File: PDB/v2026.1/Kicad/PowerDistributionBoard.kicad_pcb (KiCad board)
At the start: 2 copper layers, 171 x 112.4 mm, 75 parts, among them J1 12V_EXP3, J10 BMS, J11 IMD, J12 Suspension_Linear_Pot1, J13 Suspension_Linear_Pot2, J14 Suspension_Linear_Pot3, J15 Suspension_Linear_Pot4, J16 CCM_Faults, J17 EXP1_5V, J18 RasPI_5V, J19 LATCH_12V, J2 12V_EXP2, J20 Throttle_Sensor, J21 Current_Sensor, J24 Wheel_Sensor1, J25 Wheel_Sensor2, J26 3V3_EXP, J27 BATTERY_12V, J28 BATTERY_GND, J29 BATTERY_24V, J3 12V_EXP1, J31 FAN1_24V, J32 FAN2_24V, J33 PUMP1_24V, J34 PUMP2_24V, J35 24V_EXP1, J4 RTM, J5 CCM_12V, J7 BSPD, J8 LATCH, J9 TSSI, U1 5to3.3_Linear_Regulator, U2 TLV76150DCYR

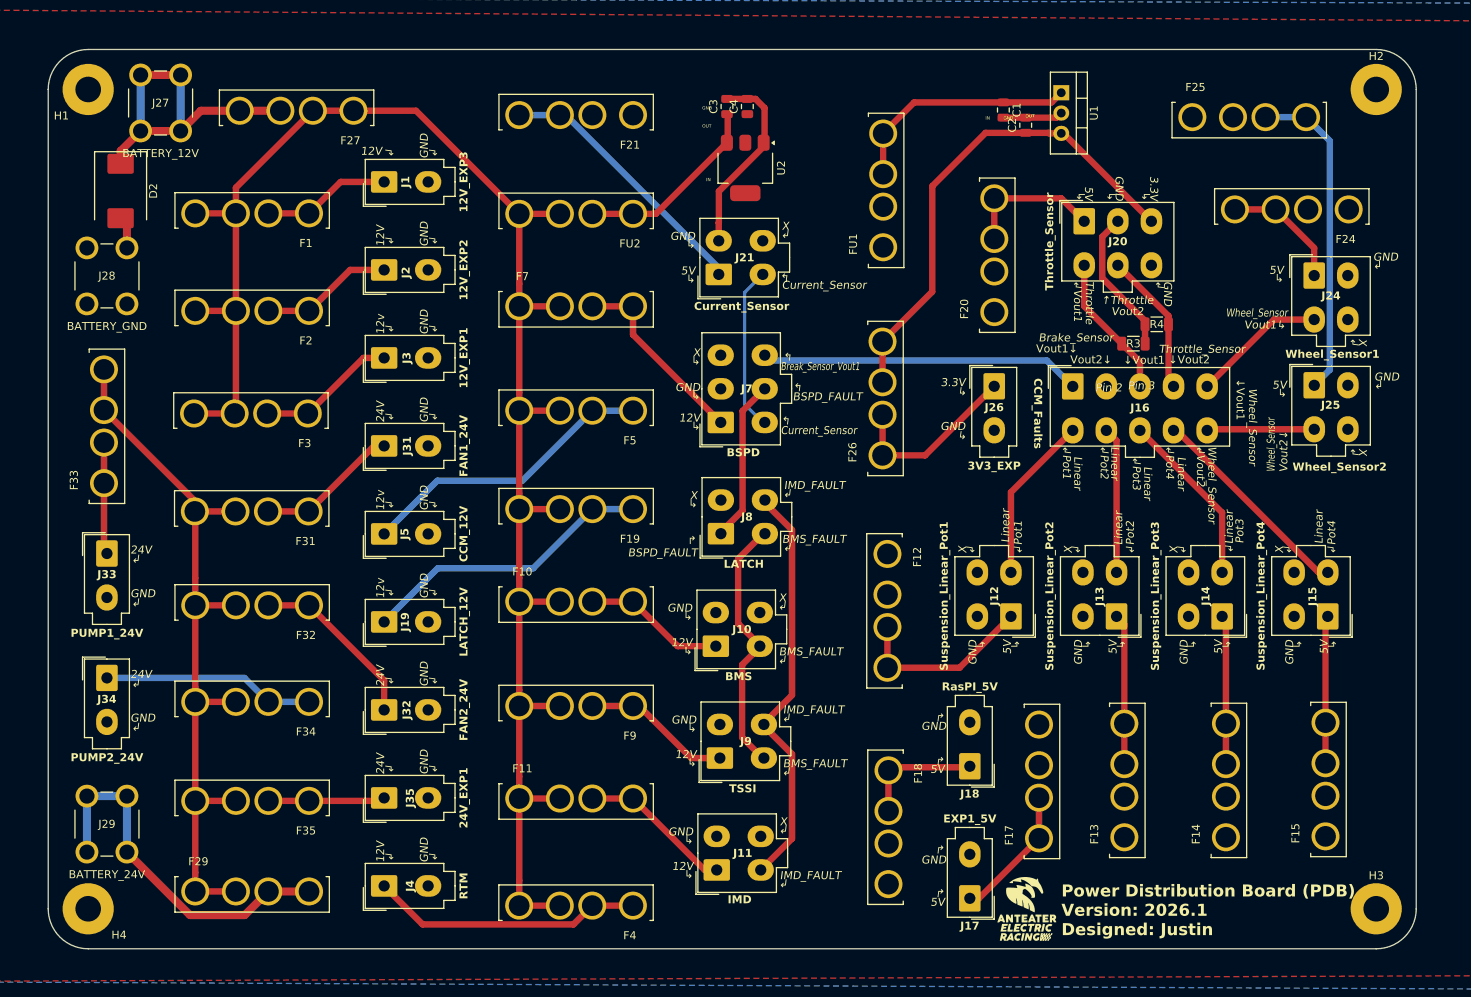
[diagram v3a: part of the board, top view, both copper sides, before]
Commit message: Shink overall board size for PDB
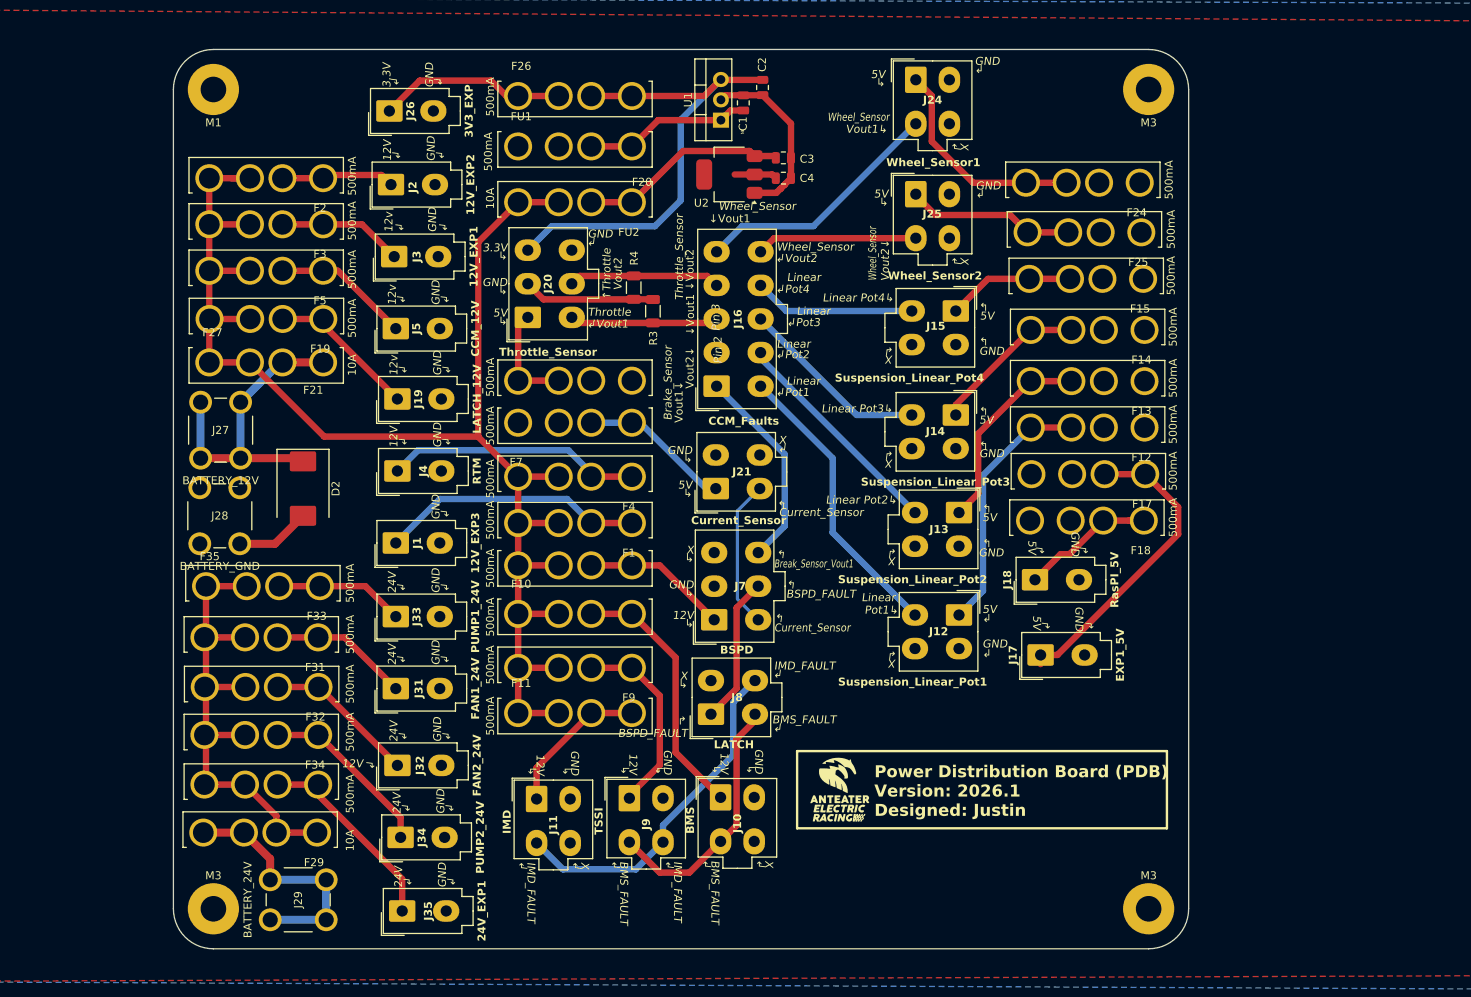
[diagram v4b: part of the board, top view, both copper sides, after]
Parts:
- added REF**: kirby, 0footprints:kirby, B.Cu at (116.1, 90.2)
- moved J26 83.1 mm to (92.8, 32.0), turned to 90 degrees
- moved J20 70.6 mm to (110.1, 57.8), turned to 90 degrees
- moved F15 69.9 mm to (179.9, 52.6), turned to 180 degrees
- moved R4 65.5 mm to (123.3, 54.1), turned to -90 degrees
- moved R3 60.2 mm to (125.7, 57.0), turned to 90 degrees
- moved J15 60.2 mm to (163.6, 57.0), turned to -90 degrees
- moved F14 59.4 mm to (180.1, 59.0), turned to 180 degrees
- moved F1 55.9 mm to (116.0, 83.1)
- moved J24 55.5 mm to (158.6, 28.1)
- moved J25 55.2 mm to (158.6, 42.4)
- moved F20 55.0 mm to (116.0, 65.3), turned to 180 degrees
- moved F26 53.9 mm to (116.0, 30.5), turned to 0 degrees
- moved F4 53.6 mm to (116.0, 77.3)
- moved J4 51.9 mm to (93.8, 77.0)
- moved F13 50.5 mm to (180.1, 65.4), turned to 180 degrees
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- renumbered H1 to M1, H4 to M3, H2 to M3, H3 to M3
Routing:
- net 24V: track 95.4 -> 63.0 mm
- net 12V: track 215.4 -> 187.9 mm
- net /Fuse_EXP1_5V: track 16.8 -> 38.9 mm
- net /Fuse_CCM_12V: track 37.5 -> 17.2 mm
- net /Fuse_Wheel2: track 40.6 -> 21.1 mm
- net /Fuse_LATCH_12V: track 36.9 -> 19.7 mm
- net /Fuse_EXP3_12V: track 16.1 -> 33.0 mm
- net Linear_Pot1: track 20.9 -> 36.6 mm
- net /Fuse_BMMS: track 17.7 -> 33.1 mm
- net /Fuse_Batt24V: track 46.2 -> 31.3 mm
- net Wheel_Sensor_Vout1: track 16.8 -> 31.5 mm
- net /Fuse_CurrentSensor: track 33.7 -> 19.0 mm
- net Brake_Sensor_Vout1: track 40.1 -> 25.7 mm
- net /Fuse_Wheel1: track 16.2 -> 27.5 mm
- net /Fuse_EXP1_24V: track 15.2 -> 25.2 mm
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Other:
- board size 171 x 112.4 mm -> 126.9 x 112.4 mm
- board text removed: "GND"
- board text removed: "OUT"

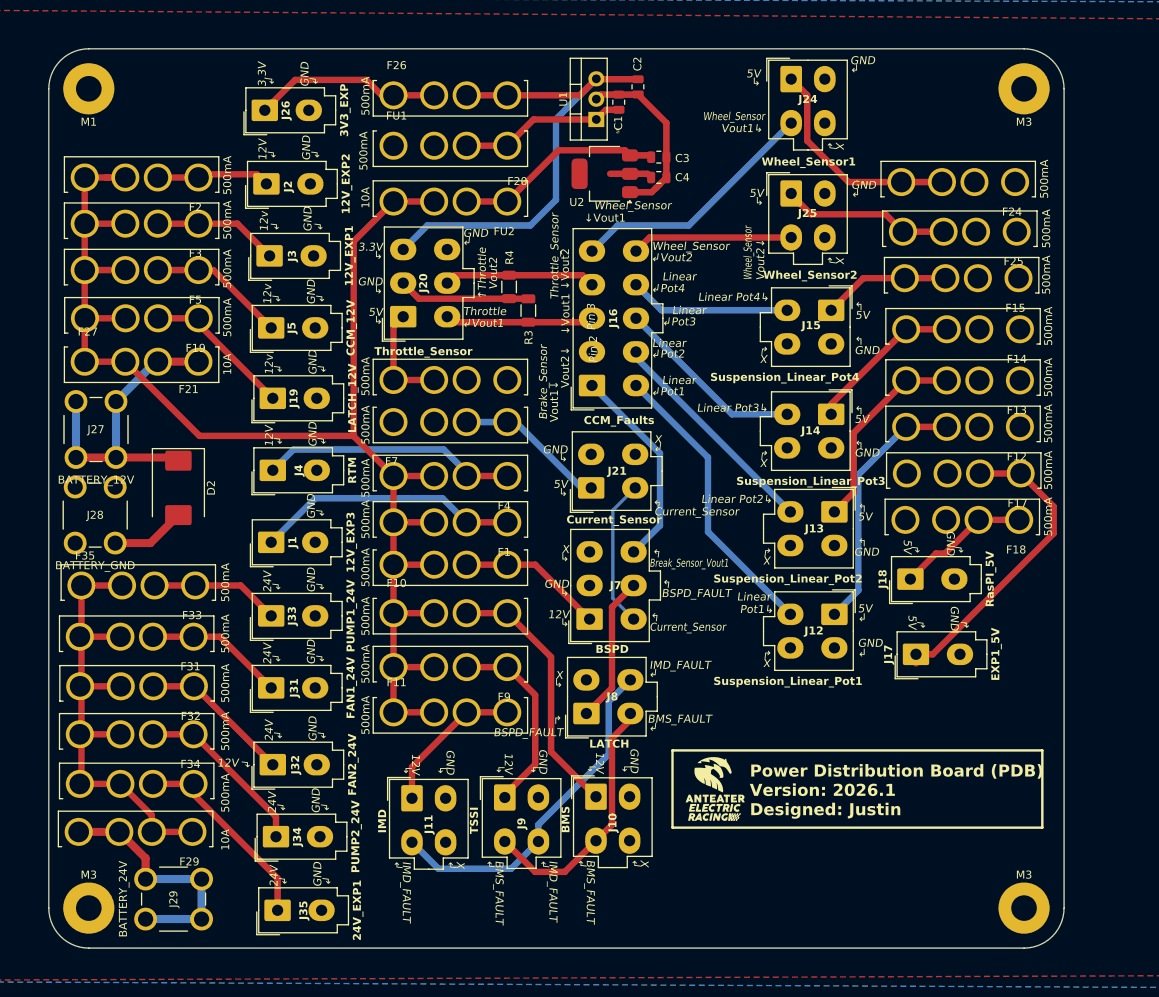
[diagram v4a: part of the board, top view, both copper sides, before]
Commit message: PDB: Removed most 5V fuses, made board size smaller
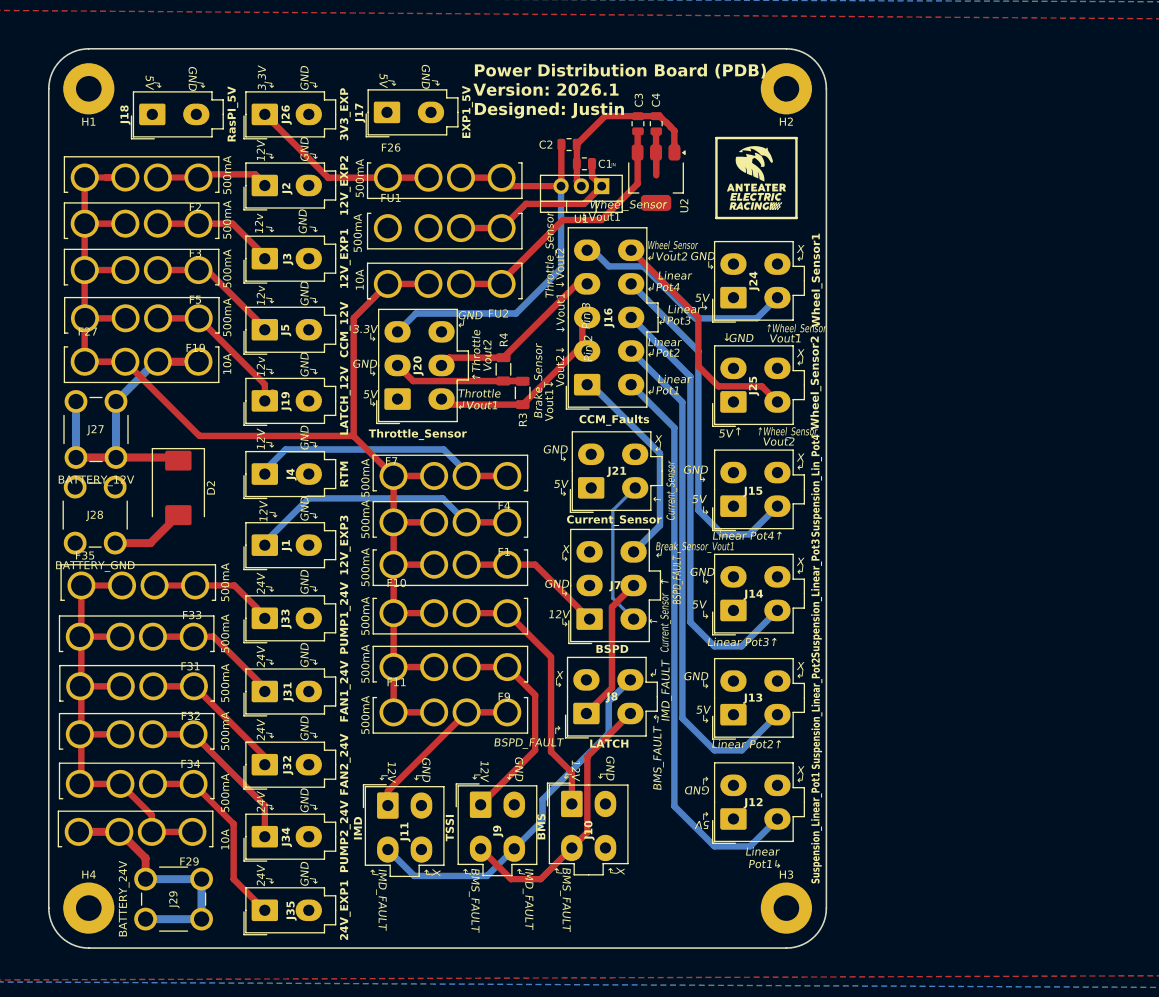
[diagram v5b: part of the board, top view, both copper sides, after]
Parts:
- removed F12, F13, F14, F15, F17, F18, F20, F21, F24, F25: 500mA, 0footprints:FUSE_3522-2
- J15: value Suspension_Linear_Pot4 -> Suspension_Lin_Pot4
- moved J18 111.1 mm to (78.7, 32.5)
- moved J17 94.7 mm to (108.1, 32.3)
- moved REF** 76.5 mm to (154.0, 40.8)
- moved H2 29.7 mm to (158.0, 29.3)
- moved H3 29.7 mm to (158.0, 131.7)
- moved J12 28.5 mm to (151.4, 120.6), turned to 90 degrees
- moved J13 28.3 mm to (151.4, 107.5), turned to 90 degrees
- moved J24 28.3 mm to (151.4, 55.4), turned to 90 degrees
- moved J14 27.4 mm to (151.4, 94.5), turned to 90 degrees
- moved J15 27.4 mm to (151.4, 81.5), turned to 90 degrees
- moved J25 27.0 mm to (151.4, 68.5), turned to 90 degrees
- moved REF** 20.8 mm to (116.8, 69.3), turned to 0 degrees
- moved C2 11.2 mm to (130.8, 36.3), turned to 0 degrees
- moved J20 10.3 mm to (109.4, 68.1)
- moved F26 10.3 mm to (115.3, 40.8)
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- renumbered M1 to H1, M3 to H2, M3 to H3, M3 to H4
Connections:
- J12 pad 1: /Fuse_Lin_Pot1 -> 5V
- J13 pad 1: /Fuse_Lin_Pot2 -> 5V
- J14 pad 1: /Fuse_Lin_Pot3 -> 5V
- J15 pad 1: /Fuse_Lin_Pot4 -> 5V
- J17 pad 1: /Fuse_EXP1_5V -> 5V
- J18 pad 1: /Fuse_RasPI_5V -> 5V
- J20 pad 1: /Fuse_Throttle -> 5V
- J21 pad 1: /Fuse_CurrentSensor -> 5V
- J24 pad 1: /Fuse_Wheel1 -> 5V
- J25 pad 1: /Fuse_Wheel2 -> 5V
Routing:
- net /Fuse_EXP1_5V: track 38.9 -> 0.00 mm
- net Linear_Pot2: track 28.0 -> 63.9 mm
- net Linear_Pot1: track 36.6 -> 71.3 mm
- net /Fuse_Lin_Pot1: track 32.2 -> 0.00 mm
- net Linear_Pot3: track 23.9 -> 55.2 mm
- net /Fuse_Wheel1: track 27.5 -> 0.00 mm
- net /Fuse_Lin_Pot2: track 25.2 -> 0.00 mm
- net Linear_Pot4: track 20.2 -> 44.4 mm
- net /Fuse_Wheel2: track 21.1 -> 0.00 mm
- net /Fuse_Lin_Pot3: track 19.6 -> 0.00 mm
- net /Fuse_CurrentSensor: track 19.0 -> 0.00 mm
- net /Fuse_RasPI_5V: track 18.8 -> 0.00 mm
- net /Fuse_Lin_Pot4: track 15.9 -> 0.00 mm
- net /Fuse_Throttle: track 13.7 -> 0.00 mm
- net 12V: track 187.9 -> 177.3 mm
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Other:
- board size 126.9 x 112.4 mm -> 97.2 x 112.4 mm

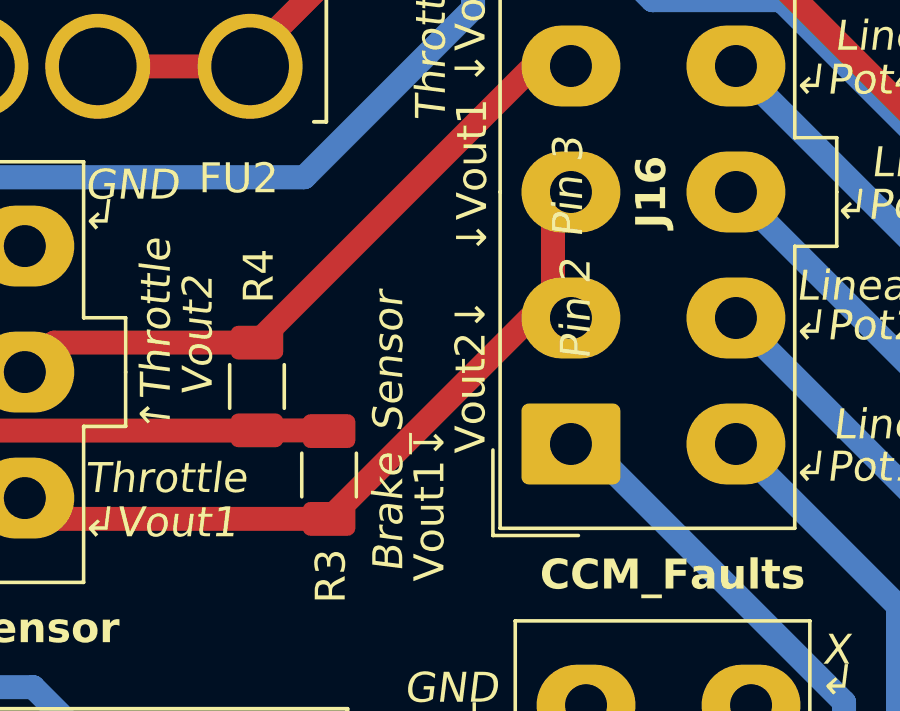
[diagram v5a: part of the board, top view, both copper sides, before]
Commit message: Major changes for PDB schematic
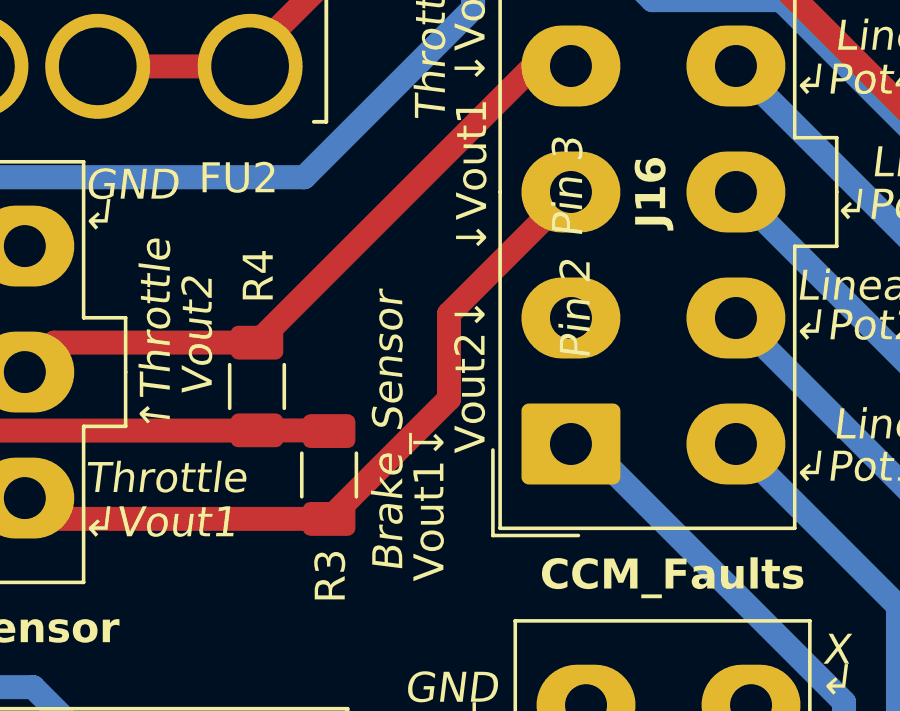
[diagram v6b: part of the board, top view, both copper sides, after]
